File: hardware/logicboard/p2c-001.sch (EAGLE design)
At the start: 46 parts, among them IC1 74LS07N, K1 G5V1, T1 2SC1815

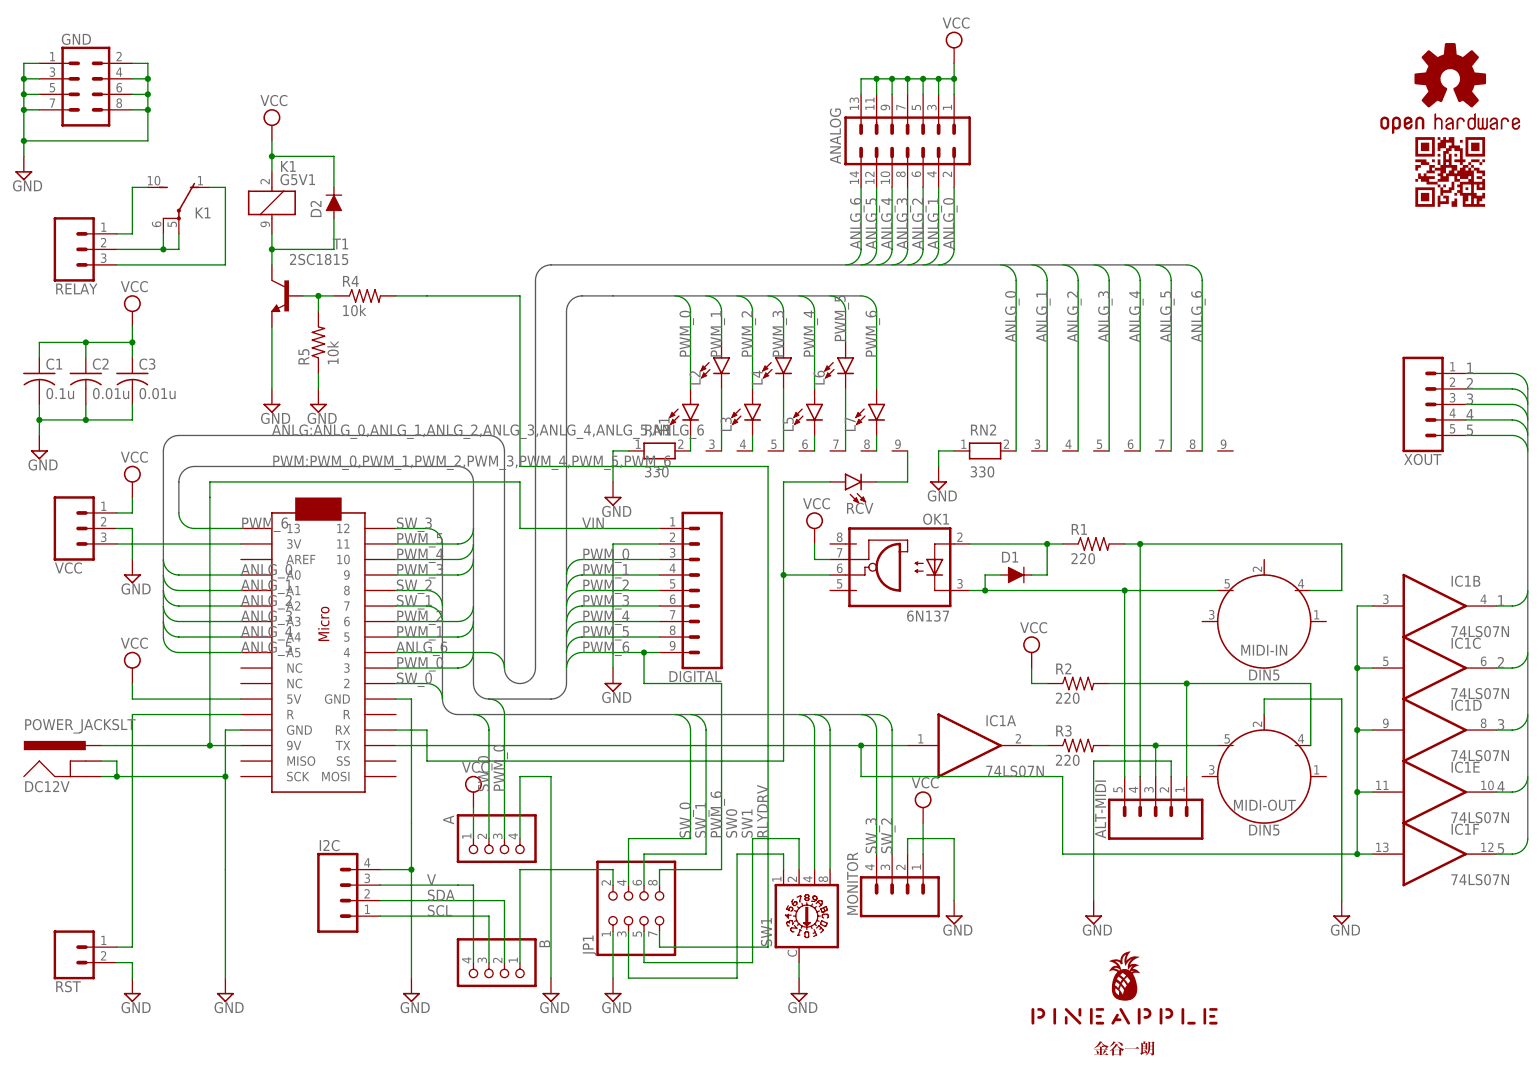
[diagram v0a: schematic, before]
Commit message: Now has Lightdrive and MKR1000-compatible I2C connector.
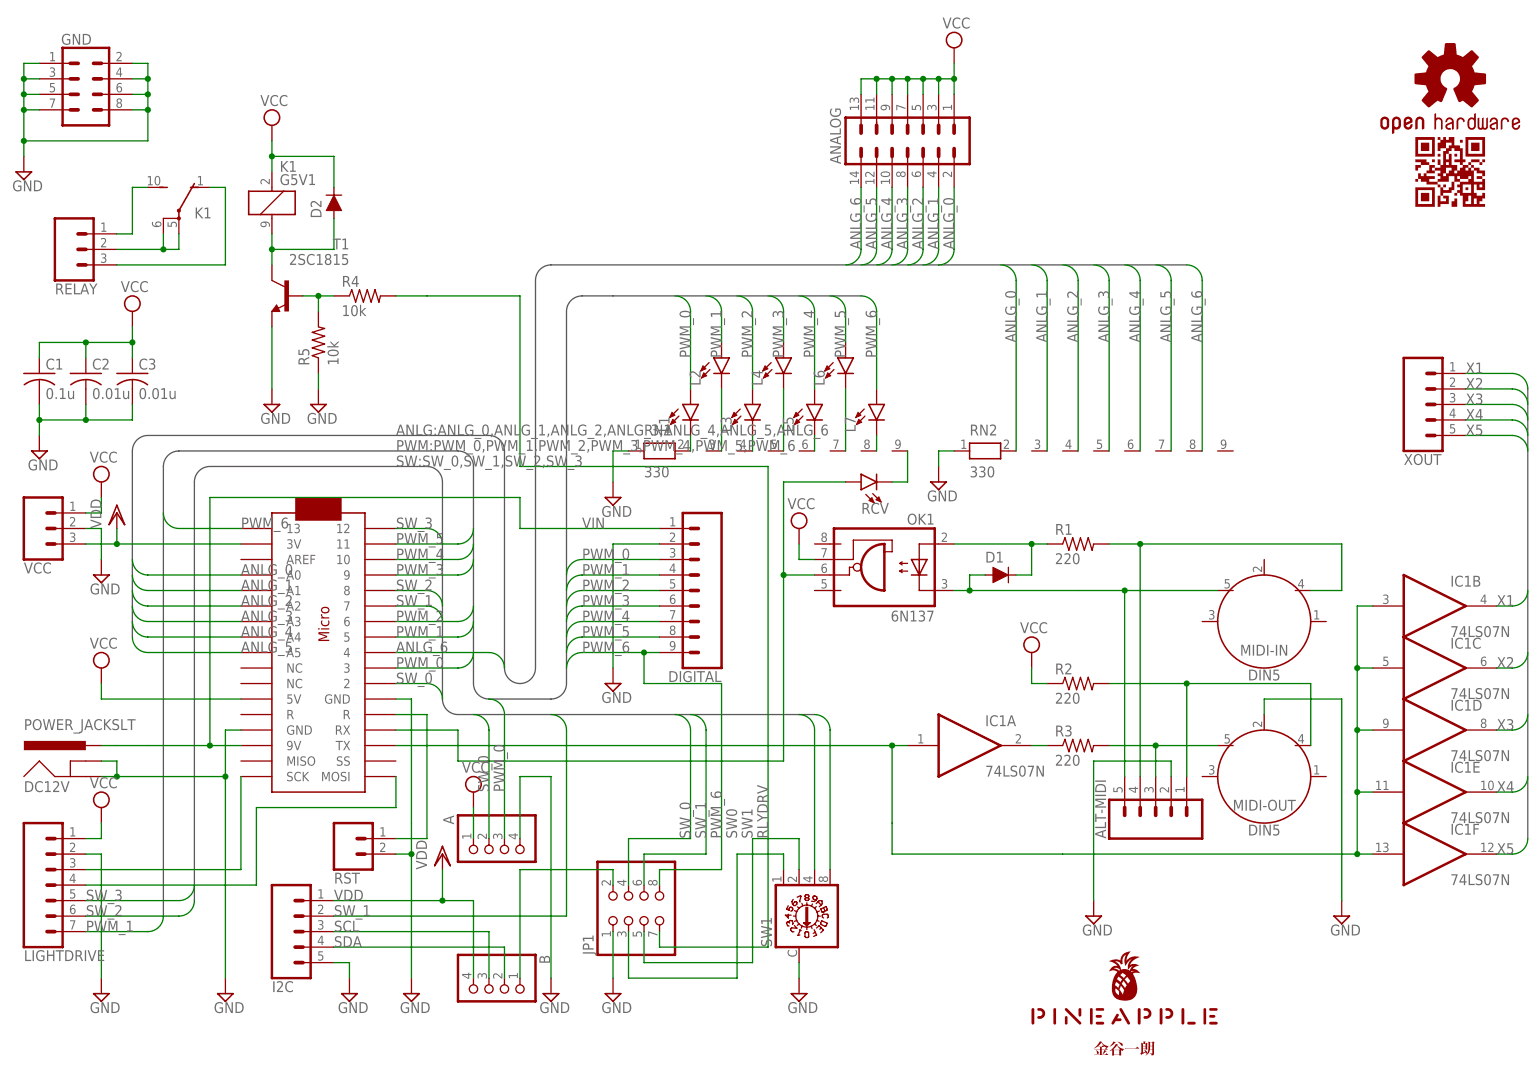
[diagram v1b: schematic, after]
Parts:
- removed MONITOR: (no value), SparkFun-Connectors:CONN_04JST-PTH-VERT
- added LIGHTDRIVE: (no value), SparkFun-Connectors:CONN_07
- I2C: device SparkFun-Connectors:CONN_04JST-PTH-VERT -> SparkFun-Connectors:CONN_05SMD2
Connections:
- net 1 renamed X1
- net 2 renamed X2
- net 3 renamed X3
- net 4 renamed X4
- net 5 renamed X5
- removed net V: B.4, I2C.3
- removed net V3: U$2.3V, VCC.3
- new net MOSI: LIGHTDRIVE.4, U$2.MOSI
- new net SCK: LIGHTDRIVE.3, U$2.SCK
- new net VDD: B.4, I2C.1, U$2.3V, VCC.3
- net GND: now also I2C.5, LIGHTDRIVE.2; no longer I2C.4, MONITOR.2
- net PWM_1: now also LIGHTDRIVE.7
- net RST: now also U$2.R@2; no longer U$2.R@1
- net SCL: now also I2C.3; no longer I2C.1
- net SDA: now also I2C.4; no longer I2C.2
- net SW_1: now also I2C.2
- net SW_2: now also LIGHTDRIVE.6; no longer MONITOR.3
- net SW_3: now also LIGHTDRIVE.5; no longer MONITOR.4
- net VCC: now also LIGHTDRIVE.1; no longer MONITOR.1
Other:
- moved on the sheet: B, D1, OK1, R1, RCV, RST, VCC

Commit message: Fixed backside notes.
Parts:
- RN2: value 330 -> 10k
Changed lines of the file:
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@@
 <setting verticaltext="up"/>
 </settings>
-<grid distance="0.1" unitdist="inch" unit="inch" style="dots" multiple="1" display="yes" altdistance="0.01" altunitdist="inch" altunit="inch"/>
+<grid distance="0.1" unitdist="inch" unit="inch" style="lines" multiple="1" display="no" altdistance="0.01" altunitdist="inch" altunit="inch"/>
 <layers>
 <layer number="1" name="Top" color="4" fill="1" visible="no" active="no"/>
@@
 <part name="RN1" library="resistor-net" library_urn="urn:adsk.eagle:library:343" deviceset="RN08" device="" package3d_urn="urn:adsk.eagle:package:24977/1" value="330"/>
 <part name="SUPPLY8" library="supply2" library_urn="urn:adsk.eagle:library:372" deviceset="VCC" device=""/>
-<part name="RN2" library="resistor-net" library_urn="urn:adsk.eagle:library:343" deviceset="RN08" device="" package3d_urn="urn:adsk.eagle:package:24977/1" value="330"/>
+<part name="RN2" library="resistor-net" library_urn="urn:adsk.eagle:library:343" deviceset="RN08" device="" package3d_urn="urn:adsk.eagle:package:24977/1" value="10k"/>
 <part name="SUPPLY9" library="supply2" library_urn="urn:adsk.eagle:library:372" deviceset="GND" device=""/>
 <part name="C1" library="resistor" library_urn="urn:adsk.eagle:library:348" deviceset="C-US" device="025-025X050" package3d_urn="urn:adsk.eagle:package:26151/1" value="0.1u"/>

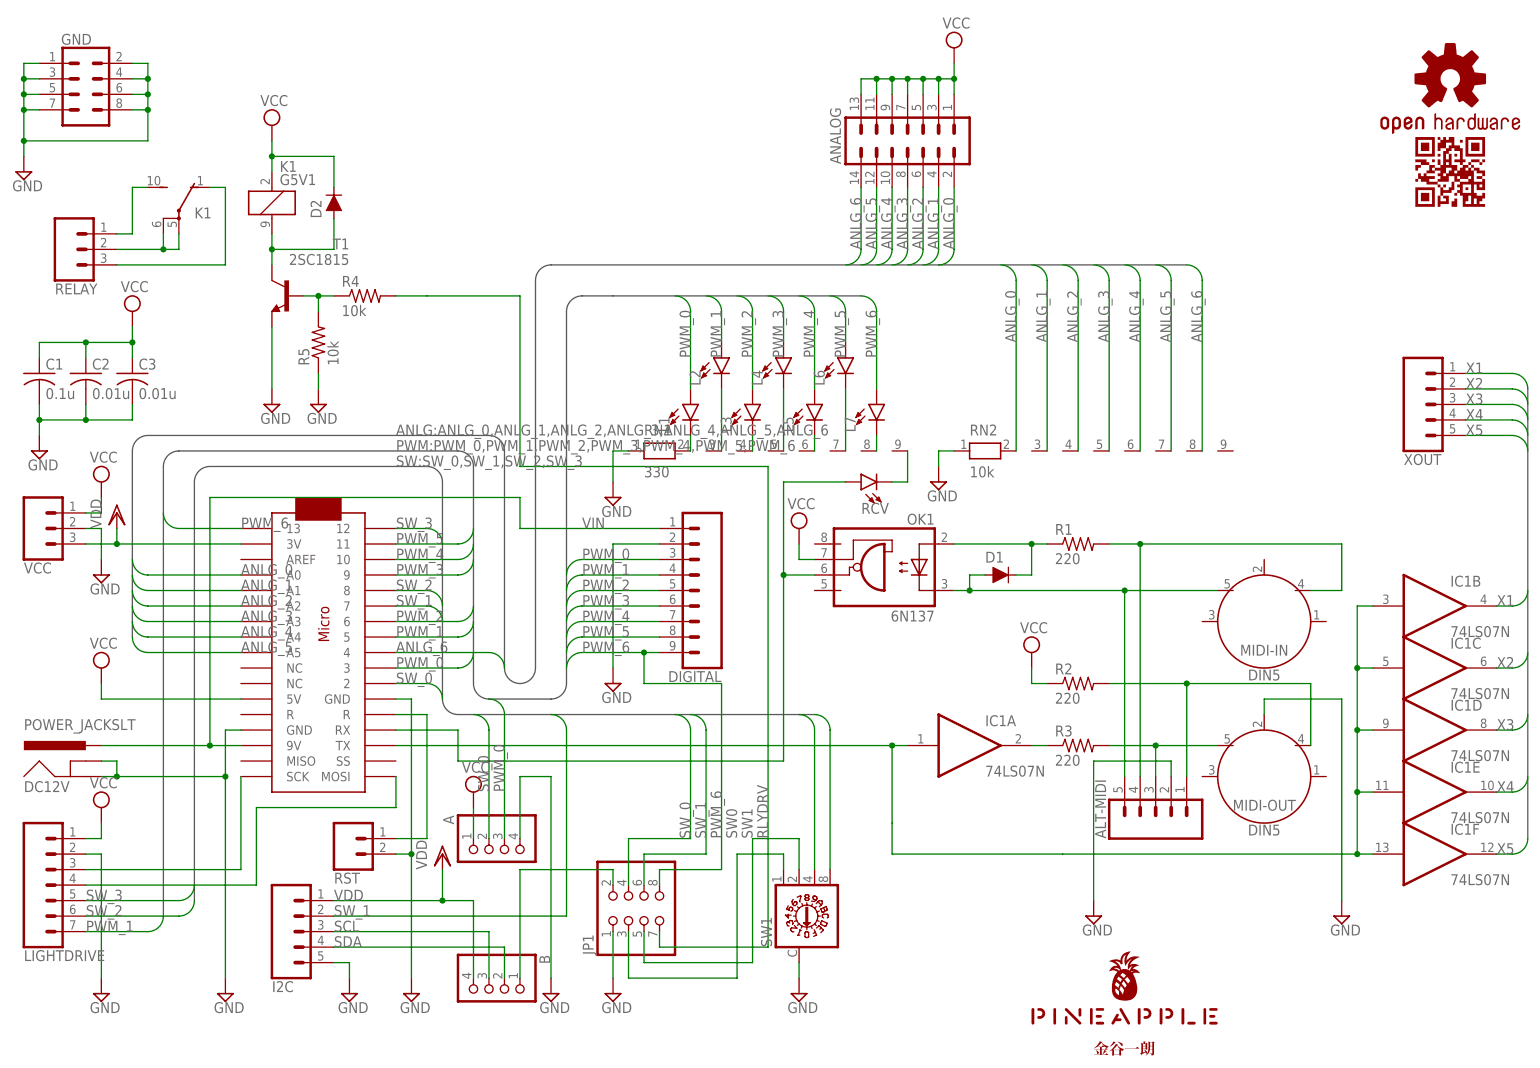
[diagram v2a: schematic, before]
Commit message: Added Pogopin.
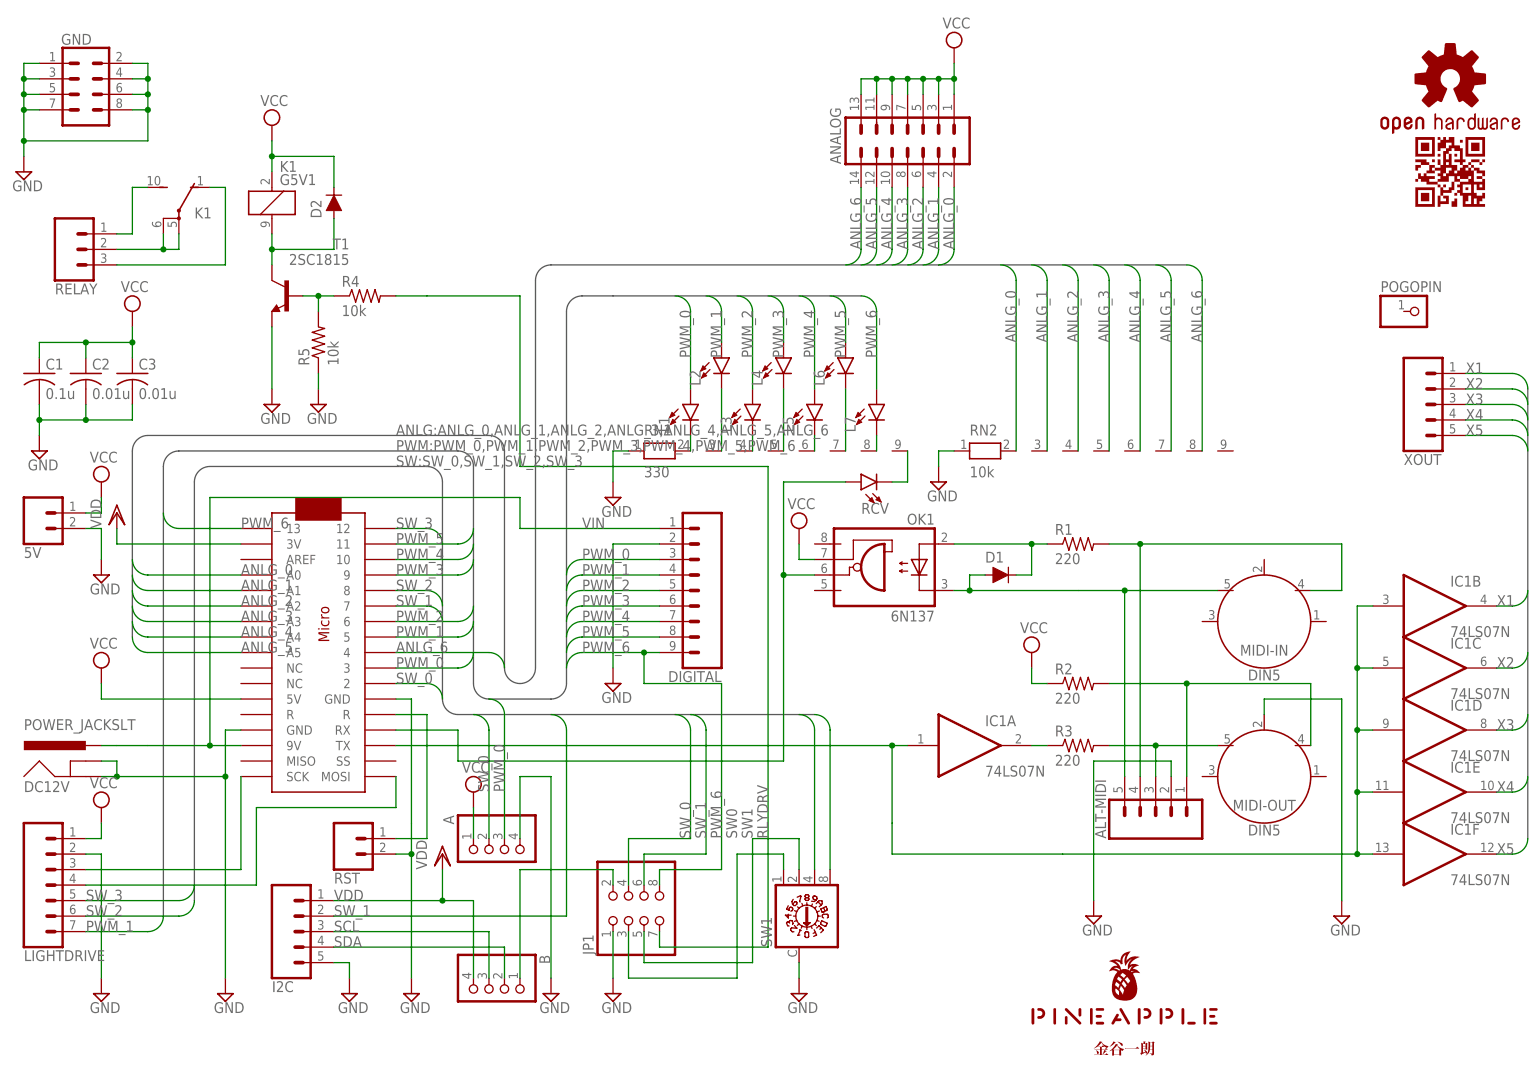
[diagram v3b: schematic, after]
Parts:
- removed VCC: (no value), SparkFun-Connectors:CONN_03
- added 5V: (no value), SparkFun-Connectors:CONN_02
- added POGOPIN: (no value), pinhead:PINHD-1X1
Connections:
- net GND: now also 5V.2; no longer VCC.2
- net VCC: now also 5V.1; no longer VCC.1
- net VDD: no longer VCC.3
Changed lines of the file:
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@@
 <part name="SUPPLY28" library="supply2" library_urn="urn:adsk.eagle:library:372" deviceset="GND" device=""/>
 <part name="GND" library="SparkFun-Connectors" library_urn="urn:adsk.eagle:library:513" deviceset="CONN_04X2" device="" package3d_urn="urn:adsk.eagle:package:38103/1"/>
-<part name="VCC" library="SparkFun-Connectors" library_urn="urn:adsk.eagle:library:513" deviceset="CONN_03" device="" package3d_urn="urn:adsk.eagle:package:38063/1"/>
 <part name="DIGITAL" library="SparkFun-Connectors" library_urn="urn:adsk.eagle:library:513" deviceset="CONN_09" device="" package3d_urn="urn:adsk.eagle:package:38153/1"/>
 <part name="XOUT" library="SparkFun-Connectors" library_urn="urn:adsk.eagle:library:513" deviceset="CONN_05" device="" package3d_urn="urn:adsk.eagle:package:38104/1"/>
@@
 <part name="VDD1" library="supply1" library_urn="urn:adsk.eagle:library:371" deviceset="VDD" device=""/>
 <part name="VDD2" library="supply1" library_urn="urn:adsk.eagle:library:371" deviceset="VDD" device=""/>
+<part name="POGOPIN" library="pinhead" library_urn="urn:adsk.eagle:library:325" deviceset="PINHD-1X1" device="" package3d_urn="urn:adsk.eagle:package:22485/2"/>
+<part name="5V" library="SparkFun-Connectors" library_urn="urn:adsk.eagle:library:513" deviceset="CONN_02" device="" package3d_urn="urn:adsk.eagle:package:38039/1"/>
 </parts>
 <sheets>
@@
 <instance part="SUPPLY28" gate="GND" x="7.62" y="149.86"/>
 <instance part="GND" gate="G$1" x="17.78" y="162.56"/>
-<instance part="VCC" gate="J$1" x="10.16" y="91.44" rot="MR180"/>
 <instance part="DIGITAL" gate="G$1" x="121.92" y="81.28" rot="R180"/>
 <instance part="XOUT" gate="G$1" x="236.22" y="111.76" rot="MR180"/>
@@
 <instance part="VDD1" gate="G$1" x="22.86" y="93.98"/>
 <instance part="VDD2" gate="G$1" x="76.2" y="38.1"/>
+<instance part="POGOPIN" gate="G$1" x="236.22" y="127"/>
+<instance part="5V" gate="G$1" x="10.16" y="93.98" rot="MR180"/>
 </instances>
 <busses>
@@
 <pinref part="SUPPLY17" gate="GND" pin="GND"/>
 <wire x1="20.32" y1="91.44" x2="20.32" y2="86.36" width="0.1524" layer="91"/>
-<pinref part="VCC" gate="J$1" pin="2"/>
+<pinref part="5V" gate="G$1" pin="2"/>
 </segment>
 <segment>
@@
 <wire x1="20.32" y1="96.52" x2="20.32" y2="93.98" width="0.1524" layer="91"/>
 <wire x1="20.32" y1="93.98" x2="17.78" y2="93.98" width="0.1524" layer="91"/>
-<pinref part="VCC" gate="J$1" pin="1"/>
+<pinref part="5V" gate="G$1" pin="1"/>
 </segment>
 <segment>
@@
 <pinref part="U$2" gate="G$1" pin="3V"/>
 <wire x1="43.18" y1="88.9" x2="22.86" y2="88.9" width="0.1524" layer="91"/>
-<pinref part="VCC" gate="J$1" pin="3"/>
 <pinref part="VDD1" gate="G$1" pin="VDD"/>
-<wire x1="22.86" y1="88.9" x2="17.78" y2="88.9" width="0.1524" layer="91"/>
 <wire x1="22.86" y1="91.44" x2="22.86" y2="88.9" width="0.1524" layer="91"/>
-<junction x="22.86" y="88.9"/>
-</segment>
-</net>
+</segment>
+</net>
